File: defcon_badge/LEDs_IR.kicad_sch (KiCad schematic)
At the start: 13 parts, among them U30 TSOP4838

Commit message: Schematic: fix +3V3 power-tree (board was dead) + add review framework
The +3V3 rail was fragmented into 5 disconnected nets — child sheets emitted it
via sheet-local (label "+3V3") while MCU_Core used global power:+3V3 symbols, so
the LDO output reached zero loads and the whole board could not power up
(6 ERC errors incl. 5 power_pin_not_driven). Root-caused and fixed at the
GENERATOR level, then regenerated the sheets:

- kicad_sheet_gen.py: RAIL_NAMES + label_at_pin() routes rail nets through the
  global power: symbol (never a sheet-local label that can't cross hierarchy).
- gen_power_sheet.py: add #FLG_GND PWR_FLAG (GND was undriven); drop redundant
  #FLG_BAT (it shorted two power outputs -> pin_to_pin error).
- gen_io_sheet.py: restore SW23 (SYNC button) + BTN_SYNC — caught generator drift
  where the committed schematic had SW23 but the generator only made 3 buttons.

Result (authoritative kicad-cli ERC/netlist): ERC 6->0 errors, +3V3 unified
(5 nets -> 1), all power pins driven, no pin conflicts. 4/5 gates pass (the 5th
is the 7 intentional RP2040 GPIO spares).

Adds schematic_phase/ — an authoritative, repeatable schematic-review framework
mirroring placement_phase_2/ (HARNESS, LEDGER, metrics.jsonl, and tools/sch_health.py
which derives all metrics from kicad-cli, not the analyzer that over-merges nets).

Co-Authored-By: Claude Opus 4.8 (1M context) <noreply@anthropic.com>
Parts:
- R30: value 68 -> 150

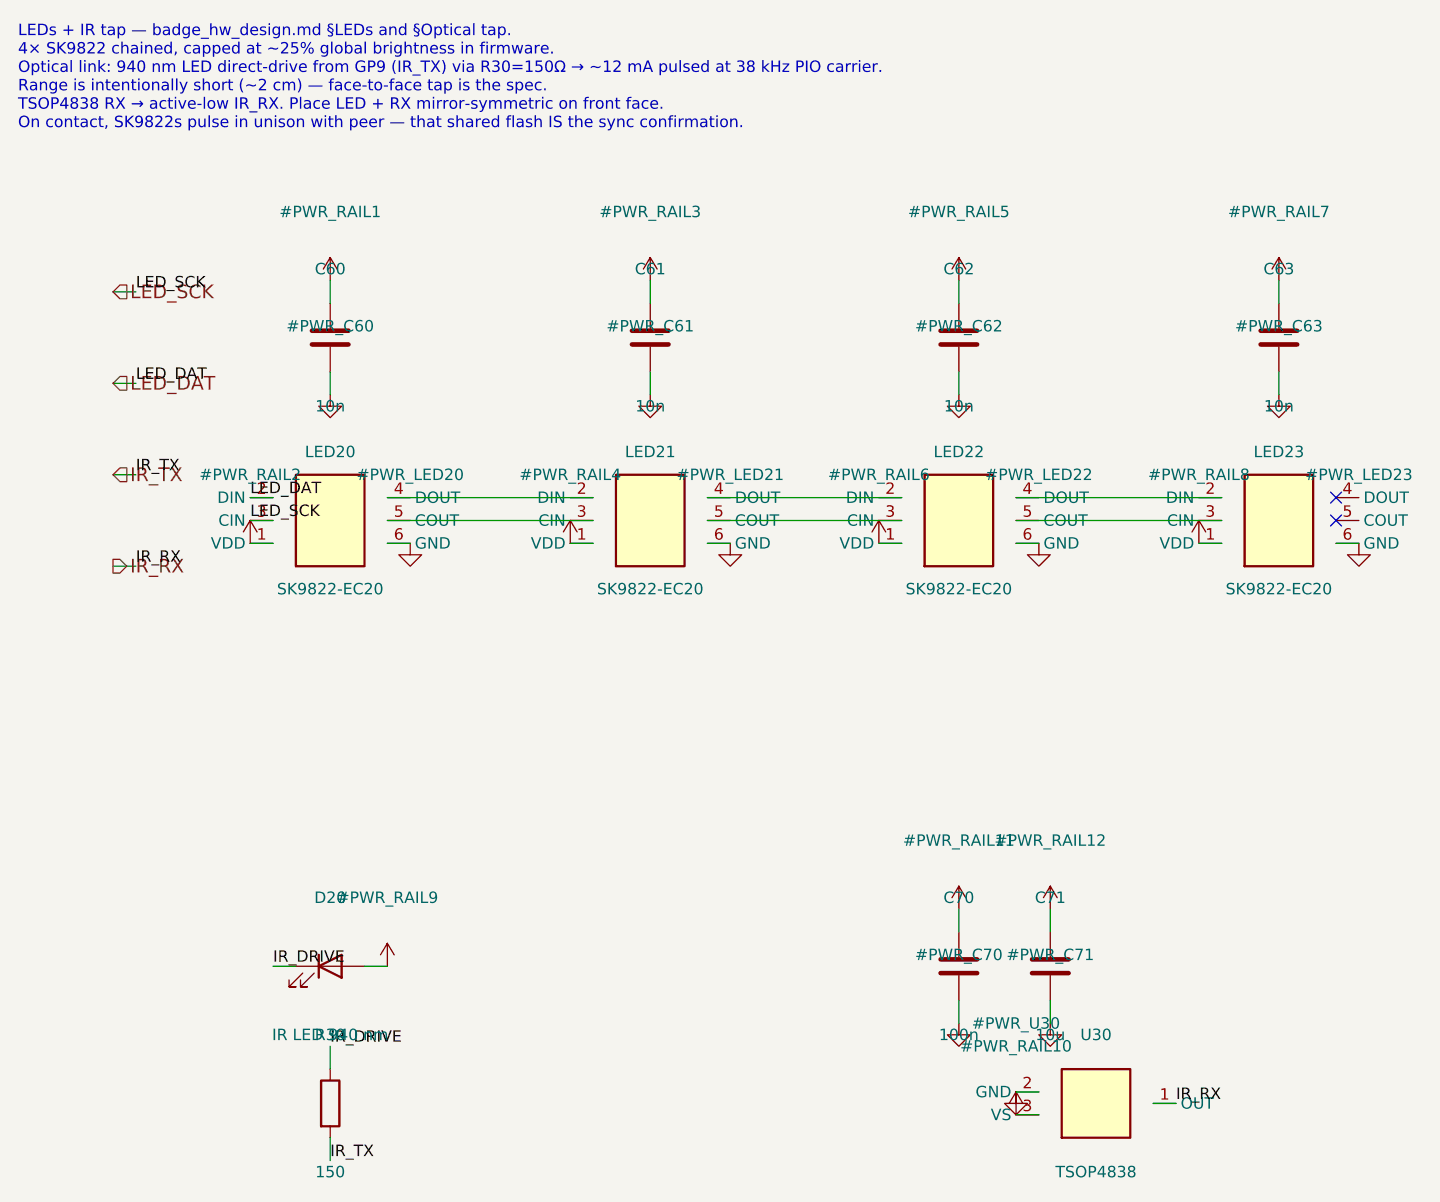
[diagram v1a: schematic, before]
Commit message: Schematic: fix TM8211 DAC + SK9822 LED pinouts (datasheet-verified)
Both were ERC-invisible symbol bugs (wrong pin-number->signal mapping) that only
datasheet cross-reference catches — the kind that ships a non-functional board.

- TM8211 DAC (U20): the symbol pinout was scrambled. Verified against the Princeton
  PT8211 datasheet (+3 cross-checks): 1=BCK 2=WS 3=DIN 4=GND 5=VDD 6=LCH 7=NC 8=RCH.
  Fixed both symbol defs (gen_badge_lib + the inline copy in gen_audio_sheet) AND
  re-mapped the U20 wiring. Netlist verified: +3V3 was landing on the bit-clock pad;
  now every I2S/analog pin is on the correct pad.
- SK9822 LEDs (LED20-23): symbol pinout scrambled AND a 4-pad SK6812 footprint on a
  6-pin part. User chose 5050 (large/bright). Verified the SK9822 5050 datasheet
  pinout (Adafruit/Pololu/Normand): 1=DIN 2=CIN 3=GND 4=VDD 5=COUT 6=DOUT. Fixed the
  symbol + re-mapped the chain wiring; netlist verified (DOUT->next DIN, COUT->next
  CIN linked). Footprint set to badge:LED_SK9822_5050 — the 6-pad 5050 land pattern
  must be created in the PCB phase (no stock KiCad addressable-5050 footprint).
- Verified W25Q16 flash is a false alarm (already correct USON-8 + pinout).

ERC still 0 errors. The +4 warnings are the deliberate SK9822-footprint TODO.

Co-Authored-By: Claude Opus 4.8 (1M context) <noreply@anthropic.com>
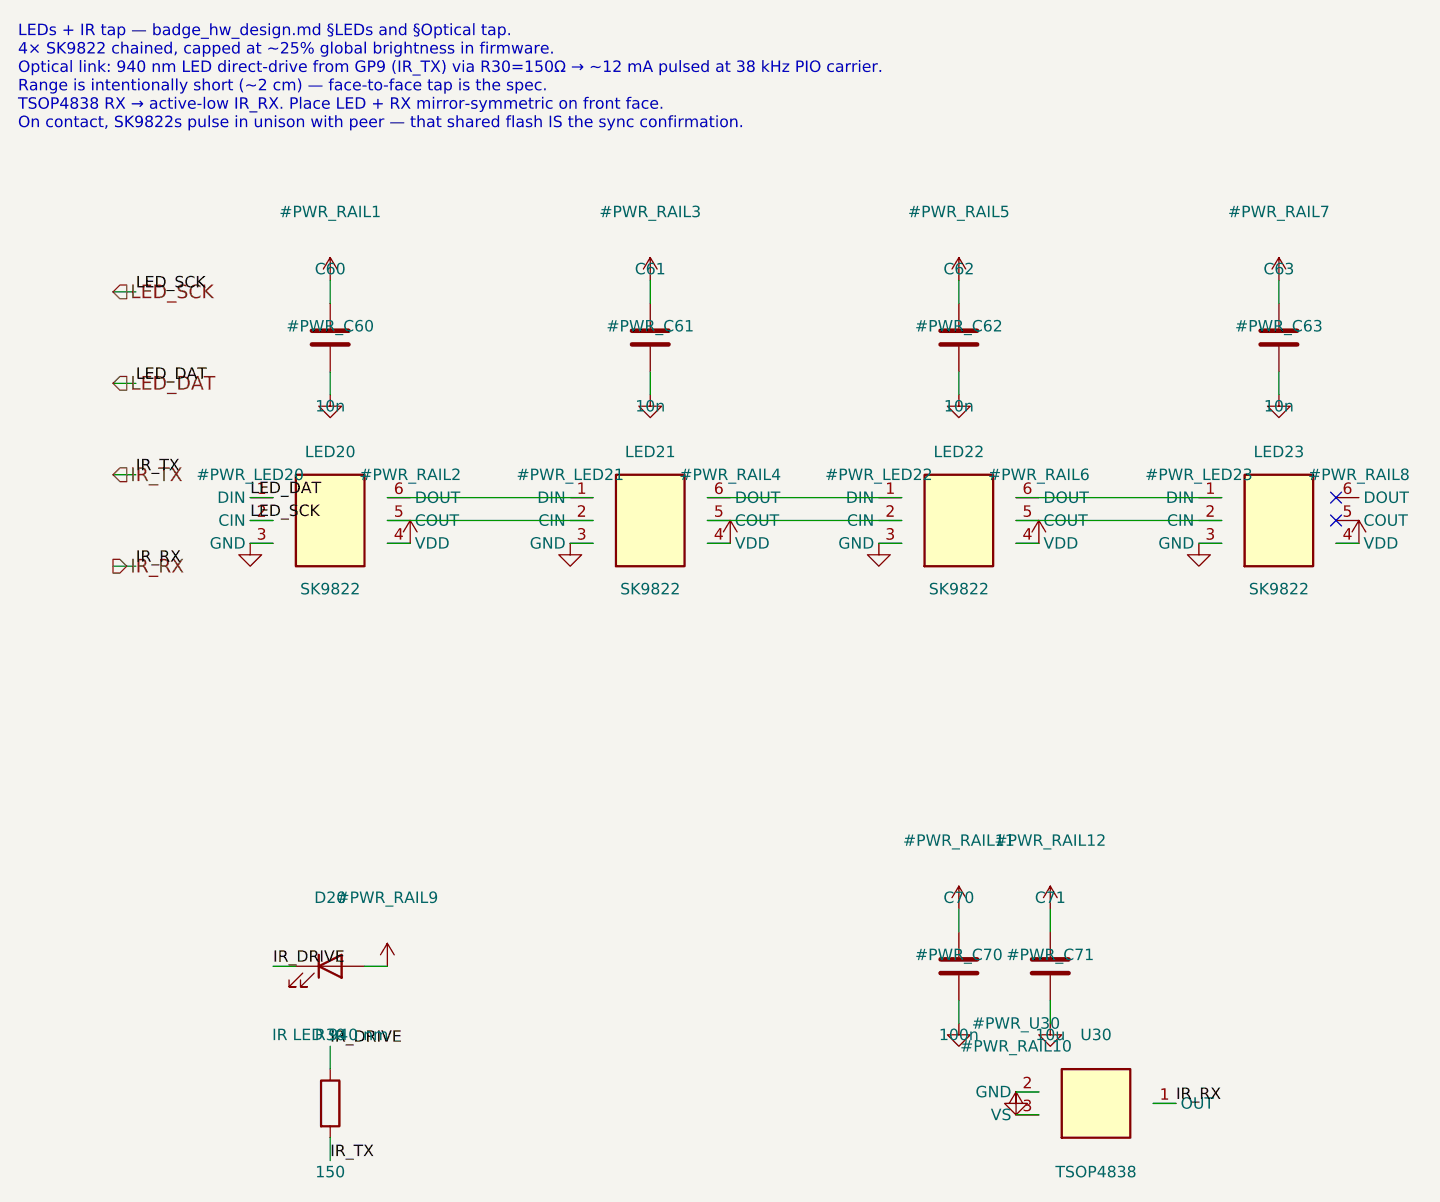
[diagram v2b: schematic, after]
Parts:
- LED20, LED21, LED22, LED23: value SK9822-EC20 -> SK9822; footprint LED_SMD:LED_SK6812_PLCC4_5.0x5.0mm_P3.2mm -> badge:LED_SK9822_5050; LCSC C2890389 -> (none); MPN SK9822-EC20 -> SK9822
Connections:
- net +3V3: now also LED20.4 (VDD), LED21.4 (VDD), LED22.4 (VDD), LED23.4 (VDD); no longer LED20.1 (VDD), LED21.1 (VDD), LED22.1 (VDD), LED23.1 (VDD)
- net GND: now also LED20.3 (GND), LED21.3 (GND), LED22.3 (GND), LED23.3 (GND); no longer LED20.6 (GND), LED21.6 (GND), LED22.6 (GND), LED23.6 (GND)
- net LED_DAT: now also LED20.1 (DIN); no longer LED20.2 (DIN)
- net LED_SCK: now also LED20.2 (CIN); no longer LED20.3 (CIN)
- net at LED21.2 (CIN): now also LED20.5 (COUT); no longer LED20.4 (DOUT)
- net at LED22.2 (CIN): now also LED21.5 (COUT); no longer LED21.4 (DOUT)
- net at LED23.2 (CIN): now also LED22.5 (COUT); no longer LED22.4 (DOUT)
- new net: LED22.6 (DOUT), LED23.1 (DIN)
- new net: LED21.6 (DOUT), LED22.1 (DIN)
- new net: LED20.6 (DOUT), LED21.1 (DIN)

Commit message: Fix 3 pin-out bugs found by the datasheet audit (D20, J30, J31)
Ran a datasheet pin-out audit (verify + adversarial cross-check) over all 18
parts with datasheet-defined pinouts. 14 verified clean. Four flagged; after
independent adjudication, three were real bugs and one a false positive:

D20 IR LED (FATAL, reverse-biased): the Everlight IR15-21C/TR8 datasheet
numbers pad 1 = ANODE, pad 2 = CATHODE — the OPPOSITE of KiCad's stock LED
convention (pad1=cathode). Under standard part-pin1 -> footprint-pad1
placement, the old wiring put the real anode on IR_DRIVE and the cathode on
+3V3, so the emitter could never forward-bias and the IR-sync TX was dead.
ERC-invisible (both pins passive). Also the footprint was 0805 for a 1206
part. Fixed: new badge:LED_IR_1206_3216Metric (pad1=anode, pad2=cathode,
cathode silk on pad 2) + swapped nets (pad1->+3V3, pad2->IR_DRIVE) + correct
1206 land + LCSC C72037->C409499. Nudged inboard for edge clearance.

J30 SAO header (FATAL for add-ons): VCC/GND were swapped vs the SAO 1.69bis
standard (badge.team: pin1=3V3, pin2=GND). A compliant SAO add-on would have
been reverse-powered. Fixed: pin1->+3V3, pin2->GND.

J31 microSD card-detect (broken feature): the Hirose DM3D-SF detect switch is
between pads 9 and 10, but the Det1 symbol exposes only pin 9 -> pad 10 floated,
so inserting a card never pulled SD_CD low. Fixed: Det2 symbol + pin 10 -> GND.

LED22 / SK9822 (FALSE POSITIVE): the audit compared against the SK9822-EC20
(a 2020 part) from a dated note in badge_hw_design.md. The board uses the 5050
SK9822 (chosen for brightness); its footprint pinout (1=DIN 2=CIN 3=GND 4=VDD
5=COUT 6=DOUT) was independently re-verified clean against the Normand Rev.07
and OPSCO 5050 datasheets. Updated the doc + generator (EC20 2020 -> 5050).

Verified: ERC 0 errors, schematic parity 0, overlaps/courtyard/offboard 0,
DRC 0 except the 28 inherent USB-C (J10) mask bridges. Top render confirms.

Co-Authored-By: Claude Opus 4.8 (1M context) <noreply@anthr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
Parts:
- D20: footprint LED_SMD:LED_0805_2012Metric -> badge:LED_IR_1206_3216Metric; LCSC C72037 -> C409499
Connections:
- net +3V3: now also D20.1 (K); no longer D20.2 (A)
- net IR_DRIVE: now also D20.2 (A); no longer D20.1 (K)
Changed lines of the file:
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@@
 		(rev "v0.1")
 		(company "")
-		(comment 1 "4× SK9822-EC20 chained, SPI1 clock+data, 25% global brightness cap (firmware)")
+		(comment 1 "4× SK9822 (5050) chained, SPI1 clock+data, 25% global brightness cap (firmware)")
 		(comment 2 "Optical tap link: 940 nm IR LED via S8050 + 68Ω; TSOP4838-class 38 kHz RX")
 		(comment 3 "LED + RX placed mirror-symmetric about vertical centerline (face-to-face mate)")
@@
 		(property "Reference" "D20" (at 59.69 121.92 0) (effects (font (size 1.27 1.27))))
 		(property "Value" "IR LED 940 nm" (at 59.69 137.16 0) (effects (font (size 1.27 1.27))))
-		(property "Footprint" "LED_SMD:LED_0805_2012Metric" (at 59.69 129.54 0) (show_name no) (hide yes) (effects (font (size 1.27 1.27))))
+		(property "Footprint" "badge:LED_IR_1206_3216Metric" (at 59.69 129.54 0) (show_name no) (hide yes) (effects (font (size 1.27 1.27))))
 		(property "Datasheet" "" (at 59.69 129.54 0) (show_name no) (hide yes) (effects (font (size 1.27 1.27))))
-		(property "Description" "940 nm IR transmit LED, 0805" (at 59.69 129.54 0) (show_name no) (hide yes) (effects (font (size 1.27 1.27))))
+		(property "Description" "940 nm IR transmit LED, 1206 (anode=pad1 per datasheet)" (at 59.69 129.54 0) (show_name no) (hide yes) (effects (font (size 1.27 1.27))))
 		(property "MPN" "IR15-21C/TR8" (at 59.69 129.54 0) (show_name no) (hide yes) (effects (font (size 1.27 1.27))))
-		(property "LCSC" "C72037" (at 59.69 129.54 0) (show_name no) (hide yes) (effects (font (size 1.27 1.27))))
+		(property "LCSC" "C409499" (at 59.69 129.54 0) (show_name no) (hide yes) (effects (font (size 1.27 1.27))))
 		(pin "1")
 		(pin "2")
@@
 	(symbol
 		(lib_id "power:+3V3")
-		(at 66.04 129.54 0)
-		(unit 1)
-		(body_style 1)
-		(exclude_from_sim no)
-		(in_bom yes)
-		(on_board yes)
-		(in_pos_files yes)
-		(dnp no)
-		(fields_autoplaced yes)
-		(property "Reference" "#PWR_RAIL9" (at 66.04 121.92 0) (effects (font (size 1.27 1.27))))
-		(property "Value" "+3V3" (at 66.04 137.16 0) (effects (font (size 1.27 1.27)) (hide yes)))
-		(property "Footprint" "" (at 66.04 129.54 0) (show_name no) (hide yes) (effects (font (size 1.27 1.27))))
-		(property "Datasheet" "" (at 66.04 129.54 0) (show_name no) (hide yes) (effects (font (size 1.27 1.27))))
-		(property "Description" "" (at 66.04 129.54 0) (show_name no) (hide yes) (effects (font (size 1.27 1.27))))
+		(at 53.34 129.54 0)
+		(unit 1)
+		(body_style 1)
+		(exclude_from_sim no)
+		(in_bom yes)
+		(on_board yes)
+		(in_pos_files yes)
+		(dnp no)
+		(fields_autoplaced yes)
+		(property "Reference" "#PWR_RAIL9" (at 53.34 121.92 0) (effects (font (size 1.27 1.27))))
+		(property "Value" "+3V3" (at 53.34 137.16 0) (effects (font (size 1.27 1.27)) (hide yes)))
+		(property "Footprint" "" (at 53.34 129.54 0) (show_name no) (hide yes) (effects (font (size 1.27 1.27))))
+		(property "Datasheet" "" (at 53.34 129.54 0) (show_name no) (hide yes) (effects (font (size 1.27 1.27))))
+		(property "Description" "" (at 53.34 129.54 0) (show_name no) (hide yes) (effects (font (size 1.27 1.27))))
 		(pin "1")
 		(instances
@@
 	(wire (pts (xy 135.89 77.47) (xy 158.75 77.47)) (stroke (width 0) (type default)))
 	(wire (pts (xy 135.89 80.01) (xy 158.75 80.01)) (stroke (width 0) (type default)))
+	(wire (pts (xy 55.88 129.54) (xy 53.34 129.54)) (stroke (width 0) (type default)))
 	(wire (pts (xy 63.50 129.54) (xy 66.04 129.54)) (stroke (width 0) (type default)))
-	(wire (pts (xy 55.88 129.54) (xy 53.34 129.54)) (stroke (width 0) (type default)))
 	(wire (pts (xy 59.69 140.97) (xy 59.69 138.43)) (stroke (width 0) (type default)))
 	(wire (pts (xy 59.69 148.59) (xy 59.69 151.13)) (stroke (width 0) (type default)))
@@
 	(label "LED_SCK" (at 50.80 80.01 0) (effects (font (size 1.27 1.27)) (justify left bottom)))
 	(label "LED_DAT" (at 50.80 77.47 0) (effects (font (size 1.27 1.27)) (justify left bottom)))
-	(label "IR_DRIVE" (at 53.34 129.54 0) (effects (font (size 1.27 1.27)) (justify left bottom)))
+	(label "IR_DRIVE" (at 66.04 129.54 0) (effects (font (size 1.27 1.27)) (justify left bottom)))
 	(label "IR_DRIVE" (at 59.69 138.43 0) (effects (font (size 1.27 1.27)) (justify left bottom)))
 	(label "IR_TX" (at 59.69 151.13 0) (effects (font (size 1.27 1.27)) (justify left bottom)))
